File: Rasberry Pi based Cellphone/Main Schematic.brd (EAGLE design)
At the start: 100 x 80 mm, 124 parts, among them IC1 PCM2904DB, J1 Main B2B Header, J2 Second B2B Header, J3 Third B2B Header, Q1 20V P-Channel Mosfet, SW1 SPST_TACT-KMR2, SW2 SPST_TACT-KMR2, SW3 SPST_TACT-KMR2, X1 679105700, X2 679105700, X3 5036-008-210-862, X4 679105700

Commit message: random commit
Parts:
- added C45, C46, C47, C48: 10nF/25V, adafruit:C0402
- added C49: (no value), adafruit:R/2012-12R
- added C50: 10uF/6.3V, adafruit:R/2012-12R
- added R16: 10k, adafruit:M0805
- added R17: 2.2k, adafruit:M0805
- added U$6: MCP1702T-1502E/CB, Microchip_By_element14_Batch_1:SOT95P255X145-3N
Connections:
- removed net 3V2/NVCC_EIM2: Q1.2
- new net MSATA_DISABLE: R16.1, X1.20
- new net N$51: C45.1, X1.23
- new net N$59: C46.1, X1.25
- new net N$60: C47.1, X1.31
- new net N$61: C48.1, X1.33
- new net V_1V5: C50.+, R17.2, U$6.2, X1.28, X1.48, X1.6
- net 3V2/NVCC_EIM0: now also C49.+, Q1.2, R16.2, U$6.3, U1.23, X1.2, X1.24, X1.39, X1.41, X1.52
- net I2C1_SCL: now also X1.30
- net I2C1_SDA: now also X1.32
- net PE: now also C49.-, C50.-, R17.1, U$6.1, X1.15, X1.18, X1.21, X1.26, X1.27, X1.29, X1.34, X1.35, X1.37, X1.4, X1.40, X1.43, X1.50, X1.9
- net POR_B: now also X1.22
- net SATA_RXN: now also C46.2
- net SATA_RXP: now also C45.2
- net SATA_TXN: now also C47.2
- net SATA_TXP: now also C48.2

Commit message: almost finished schematic
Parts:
- removed X2, X4: 679105700, con-molex:679105700
- added C100, C101, C102, C104, C105, C106, C107, C108, C109, C110, C111, C112, C117, C118, C119, C120, C121, C122, C123, C124, C125, C126, C127, C59, C61, C62, C63, C69, C71, C72, C73, C74, C79, C81, C82, C83, C84, C89, C91, C92, C93, C98, C99: 0.1uF, resistor:C0402
- added C103, C113, C114, C115, C116, C60, C67, C70, C75, C78, C80, C85, C88, C90, C94, C95, C96, C97: 0.001uF, resistor:C0402
- added C51, C52: 10uF/6.3V, adafruit:R/2012-12R
- added C53, C54, C55, C56, C57, C58: 0.1uF/16V, adafruit:R/2012-12R
- added C66, C76, C86: 1.0uF, resistor:C0402
- added C68, C77, C87: 0.01uF, resistor:C0402
- added L10, L11, L4, L5, L6, L7: 1000@100MHz, dp_devices:FB402
- added L8: (no value), dp_devices:FB402
- added MSATA, PCIE1, PCIE2: 679105700, con-molex:679105700
- added R18, R19, R20, R22: 2.2k, adafruit:M0805
- added R21: 1kΩ, adafruit:M0805
- added RT13, RT14, RT17, RT18, RT21, RT22: 20Ω, adafruit:M0805
- added RT15, RT16, RT19, RT20, RT23, RT24: 49.9Ω, adafruit:M0805
- added RT25, RT26, RT27: 4.7kΩ, adafruit:M0805
- added RT28: 1.6kΩ, adafruit:M0805
- added U$7: MCP1700T-1502E/TT, Microchip_By_element14_Batch_1:SOT95P237X112-3N
- added U7: XIO3130_ZHC_196, texas:ZHC196
- X1: value 679105700 -> 5036-008-210-862; device con-molex:679105700 -> con-kyocera-elco:5036_008_210_862
- moved C49 602.6 mm to (45.7, 54.6)
- moved C50 602.6 mm to (45.7, 50.8)
- moved R17 602.6 mm to (45.7, 47.0)
- moved SW3 566.7 mm to (48.3, 55.9)
- moved U$6 566.7 mm to (52.1, 24.1)
- moved C45 566.7 mm to (47.0, 50.8)
- moved C46 566.7 mm to (47.0, 47.0)
- moved C47 566.7 mm to (47.0, 43.2)
- moved C48 566.7 mm to (47.0, 39.4)
- moved R16 566.7 mm to (48.3, 33.0)
- moved SW1 566.7 mm to (48.3, 63.5)
- moved SW2 566.7 mm to (48.3, 59.7)
- moved C44 520.3 mm to (27.9, 34.3)
- moved RN1 520.3 mm to (27.9, 26.7)
- moved C42 520.3 mm to (26.7, 52.1)
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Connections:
- removed net 3V2/NVCC_EIM0: ADC/DAC.20, ADC/DAC.5, C12.-, C17.+, C23.-, C49.+, J1.P$63, J1.P$65, J1.P$67, J1.P$69, L2.2, L3.1, Q1.2, R14.1, R16.2, RT5.2, SD2_VSELECT.7, SD2_VSELECT.8, U$2.3, U$6.3, U1.23, U1.34, U1.37, U1.38, U1.47, U4.P$5, U5.P$5, U6.P$5, X1.2, X1.24, X1.39, X1.41, X1.52
- new net 12C3_SDA: GPIOB.3
- new net 1V5: C102.1, C104.1, C105.1, C106.1, C107.1, C108.1, C109.1, C110.1, C111.1, C112.1, C113.1, C114.1, C115.1, C116.1, C117.1, C118.1, C119.1, C120.1, C121.1, C122.1, C123.1, C124.1, C125.1, C126.1, C127.1, C52.+, C59.1, C69.1, C79.1, C89.1, L4.1, L5.1, L6.1, L7.1, L8.1, PCIE1.28, PCIE1.48, PCIE1.6, PCIE2.28, PCIE2.48, PCIE2.6, R18.2, U$7.2, U7.A13, U7.A4, U7.B10, U7.B12, U7.B2, U7.B3, U7.B7, U7.C11, U7.C13, U7.C14, U7.C5, U7.E13, U7.F1, U7.F2, U7.G13, U7.H3, U7.K4, U7.L14, U7.M1, U7.M11, U7.M12, U7.M2, U7.N10, U7.N13, U7.N14, U7.N8, U7.P14, U7.P3, U7.P4
- new net 3V2: ADC/DAC.20, ADC/DAC.5, C100.1, C101.1, C12.-, C17.+, C23.-, C49.+, C51.+, C74.1, C84.1, C94.1, C95.1, C96.1, C97.1, C98.1, C99.1, GPIOA.1, GPIOB.1, J1.P$63, J1.P$65, J1.P$67, J1.P$69, L10.1, L11.1, L2.2, L3.1, MSATA.2, MSATA.24, MSATA.39, MSATA.41, MSATA.52, PCIE1.2, PCIE1.24, PCIE1.39, PCIE1.41, PCIE1.52, PCIE2.2, PCIE2.24, PCIE2.39, PCIE2.41, PCIE2.52, Q1.2, R14.1, R16.2, R19.1, R20.1, R21.2, R22.1, RT5.2, SD2_VSELECT.7, SD2_VSELECT.8, U$2.3, U$6.3, U$7.3, U1.23, U1.34, U1.37, U1.38, U1.47, U4.P$5, U5.P$5, U6.P$5, U7.A11, U7.A3, U7.B4, U7.D12, U7.D4, U7.K12, U7.M4, U7.N1, U7.P11
- new net DN1_PERST: PCIE1.22, RT27.2, U7.B5
- new net DN2_PERST: PCIE2.22, RT25.2, U7.A2
- new net DN3_PERST: RT26.2, U7.A1
- new net N$62: C54.-, PCIE2.31
- new net N$63: C53.-, PCIE2.33
- new net N$66: C56.-, PCIE1.31
- new net N$67: C55.-, PCIE1.33
- new net N$75: C57.+, U7.L2
- new net N$77: C58.+, U7.L1
- new net N$79: GPIOB.12
- new net N$80: GPIOB.13
- new net PCIE_RXM1: PCIE1.23, U7.B6
- new net PCIE_RXM2: PCIE2.23, U7.F14
- new net PCIE_RXM3: U7.P9
- new net PCIE_RXP1: PCIE1.25, U7.A6
- new net PCIE_RXP2: PCIE2.25, U7.F13
- new net PCIE_RXP3: U7.N9
- new net PCIE_TXM1: C56.+, U7.B8
- new net PCIE_TXM2: C54.+, U7.H14
- new net PCIE_TXM3: U7.P7
- new net PCIE_TXP1: C55.+
- new net PCIE_TXP2: C53.+, U7.H13
- new net PCIE_TXP3: U7.N7
- new net REFCLKN_1: PCIE1.11, RT14.2, RT16.1
- new net REFCLKN_1_R: RT14.1, U7.B9
- new net REFCLKN_2: PCIE2.11, RT22.2, RT24.1
- new net REFCLKN_2_R: RT22.1, U7.J14
- new net REFCLKN_3: RT18.2, RT20.1
- new net REFCLKN_3_R: RT18.1, U7.P6
- new net REFCLKP_1: PCIE1.13, RT13.2, RT15.1
- new net REFCLKP_1_R: RT13.1, U7.A9
- new net REFCLKP_2: PCIE2.13, RT21.2, RT23.1
- new net REFCLKP_2_R: RT21.1, U7.K14
- new net REFCLKP_3: RT17.2, RT19.1
- new net REFCLKP_3_R: RT17.1, U7.P5
- new net RXD0: GPIOA.9, R20.2, U4.P$3
- new net RXD1: GPIOA.11, R19.2, U5.P$3
- new net RXD2: GPIOA.13, R22.2, U6.P$3
- new net TXD0: GPIOA.8, U4.P$6
- new net TXD1: GPIOA.10, U5.P$6
- new net TXD2: GPIOA.12, U6.P$6
- new net UIM_AUX1_1: X3.C6
- new net UIM_AUX1_2: X1.C6
- new net UIM_AUX2_1: X3.C8
- new net UIM_AUX2_2: X1.C8
- new net UIM_CLK_1: PCIE1.12, X3.C2
- new net UIM_CLK_2: PCIE2.12, X1.C2
- new net UIM_DATA_1: PCIE1.10, X3.C4
- new net UIM_DATA_2: PCIE2.10, X1.C4
- new net UIM_PWR_1: PCIE1.8, X3.C1
- new net UIM_PWR_2: PCIE2.8, X1.C1
- new net UIM_RST_1: PCIE1.14, X3.C5
- new net UIM_RST_2: PCIE2.14, X1.C5
- new net UIM_VPP_1: PCIE1.16, X3.C7
- new net UIM_VPP_2: PCIE2.16, X1.C7
- new net VAUX33REF: R21.1, U7.E1
- new net VDD15REF: C103.1, L8.2, U7.F3
- new net VDD33REF: C85.1, L11.2, U7.E2
- new net VDDA15_0: C60.1, C61.1, C62.1, C63.1, L4.2, U7.G4, U7.H2, U7.H4, U7.J4, U7.K3
- new net VDDA15_1: C70.1, C71.1, C72.1, C73.1, L5.2, U7.A7, U7.D7, U7.D8, U7.D9
- new net VDDA15_2: C80.1, C81.1, C82.1, C83.1, L6.2, U7.G11, U7.G12, U7.H11, U7.J11, U7.J12
- new net VDDA15_3: C90.1, C91.1, C92.1, C93.1, L7.2, U7.L6, U7.L7, U7.L8, U7.M6, U7.M8
- new net VDDA33F: C75.1, L10.2, U7.J3
- new net VDDCOMB15: C86.1, C87.1, C88.1, U7.C1
- new net VDDCOMB33: C76.1, C77.1, C78.1, U7.F4
- new net VDDCOMBIO: C66.1, C67.1, C68.1, U7.D3
- net +5V: now also GPIOA.2, GPIOB.2
- net CLK1_N: now also C57.-
- net CLK1_P: now also C58.-
- net DISP1_DATA00: now also EXT_RADIO_INTERFACE.3
- net DISP1_DATA01: now also EXT_RADIO_INTERFACE.2
- net DISP1_DATA02: now also GPIOB.8
- net DISP1_DATA03: now also GPIOB.9
- net DISP1_DATA04: now also GPIOB.10
- net DISP1_DATA05: now also RT28.2, U7.B1
- net DISP1_DATA06: now also GPIOB.11
- net ECSPI2_MISO: now also GPIOA.4
- net ECSPI2_MOSI: now also GPIOA.3
- net ECSPI2_SCLK: now also GPIOA.5
- net ECSPI2_SS0: now also GPIOA.6
- net ECSPI2_SS1: now also GPIOA.7
- net I2C1_SCL: now also MSATA.30, U7.B14; no longer X1.30
- net I2C1_SDA: now also MSATA.32, U7.D13; no longer X1.32
- net I2C3_SCL: now also GPIOB.4
- net MSATA_DISABLE: now also MSATA.20, PCIE1.20, PCIE2.20; no longer X1.20
- net N$51: now also MSATA.23; no longer X1.23
- net N$59: now also MSATA.25; no longer X1.25
- net N$60: now also MSATA.31; no longer X1.31
- net N$61: now also MSATA.33; no longer X1.33
- net PCIE_RXM: now also U7.J2
- net PCIE_RXP: now also U7.J1
- net PCIE_TXM: now also U7.G2
- net PCIE_TXP: now also U7.A8, U7.G1
- net PE: now also C100.2, C101.2, C102.2, C103.2, C104.2, C105.2, C106.2, C107.2, C108.2, C109.2, C110.2, C111.2, C112.2, C113.2, C114.2, C115.2, C116.2, C117.2, C118.2, C119.2, C120.2, C121.2, C122.2, C123.2, C124.2, C125.2, C126.2, C127.2, C51.-, C52.-, C59.2, C60.2, C61.2, C62.2, C63.2, C66.2, C67.2, C68.2, C69.2, C70.2, C71.2, C72.2, C73.2, C74.2, C75.2, C76.2, C77.2, C78.2, C79.2, C80.2, C81.2, C82.2, C83.2, C84.2, C85.2, C86.2, C87.2, C88.2, C89.2, C90.2, C91.2, C92.2, C93.2, C94.2, C95.2, C96.2, C97.2, C98.2, C99.2, EXT_RADIO_INTERFACE.1, GPIOA.14, GPIOB.14, MSATA.15, MSATA.18, MSATA.21, MSATA.26, MSATA.27, MSATA.29, MSATA.34, MSATA.35, MSATA.37, MSATA.4, MSATA.40, MSATA.43, MSATA.50, MSATA.9, PCIE1.15, PCIE1.18, PCIE1.21, PCIE1.26, PCIE1.27, PCIE1.29, PCIE1.34, PCIE1.35, PCIE1.37, PCIE1.4, PCIE1.40, PCIE1.43, PCIE1.50, PCIE1.9, PCIE2.15, PCIE2.18, PCIE2.21, PCIE2.26, PCIE2.27, PCIE2.29, PCIE2.34, PCIE2.35, PCIE2.37, PCIE2.4, PCIE2.40, PCIE2.43, PCIE2.50, PCIE2.9, R18.1, RT15.2, RT16.2, RT19.2, RT20.2, RT23.2, RT24.2, RT25.1, RT26.1, RT27.1, RT28.1, U$7.1, U7.A10, U7.A5, U7.C10, U7.C4, U7.C7, U7.C8, U7.C9, U7.D1, U7.D10, U7.D11, U7.D5, U7.D6, U7.E10, U7.E11, U7.E12, U7.E14, U7.E4, U7.E5, U7.E6, U7.E7, U7.E8, U7.E9, U7.F10, U7.F11, U7.F12, U7.F5, U7.F6, U7.F7, U7.F8, U7.F9, U7.G10, U7.G14, U7.G3, U7.G5, U7.G6, U7.G7, U7.G8, U7.G9, U7.H1, U7.H10, U7.H12, U7.H5, U7.H6, U7.H7, U7.H8, U7.H9, U7.J10, U7.J13, U7.J5, U7.J6, U7.J7, U7.J8, U7.J9, U7.K1, U7.K10, U7.K11, U7.K13, U7.K2, U7.K5, U7.K6, U7.K7, U7.K8, U7.K9, U7.L10, U7.L11, U7.L13, U7.L4, U7.L5, U7.L9, U7.M5, U7.M7, U7.M9, U7.N4, U7.N5, U7.N6, U7.P1, U7.P10, U7.P8, X1.C3, X3.C3; no longer X1.15, X1.18, X1.21, X1.26, X1.27, X1.29, X1.34, X1.35, X1.37, X1.4, X1.40, X1.43, X1.50, X1.9
- net POR_B: now also MSATA.22; no longer X1.22
- net SD3_CLK: now also GPIOB.6
- net SD3_CMD: now also GPIOB.7
- net UART1_RX_DATA: now also U4.P$4
- net UART1_TX_DATA: now also U4.P$1
- net UART2_RX_DATA: now also U5.P$4
- net UART2_TX_DATA: now also U5.P$1
- net UART3_RX_DATA: now also U6.P$4
- net UART3_TX_DATA: now also U6.P$1
- net USB_OTG_ID: now also GPIOB.5
- net V_1V5: now also MSATA.28, MSATA.48, MSATA.6; no longer X1.28, X1.48, X1.6

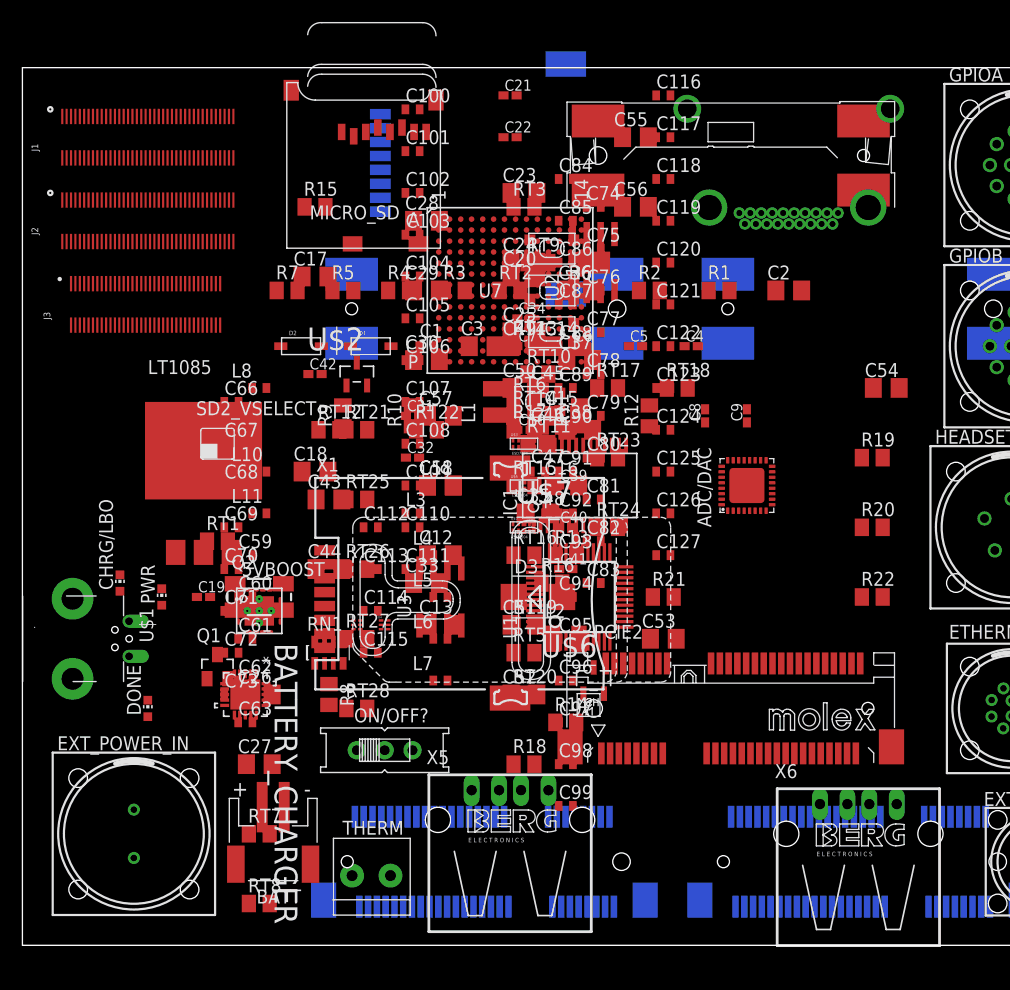
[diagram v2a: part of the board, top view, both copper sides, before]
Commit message: fixed some errors in schematic and made brd easier to look at
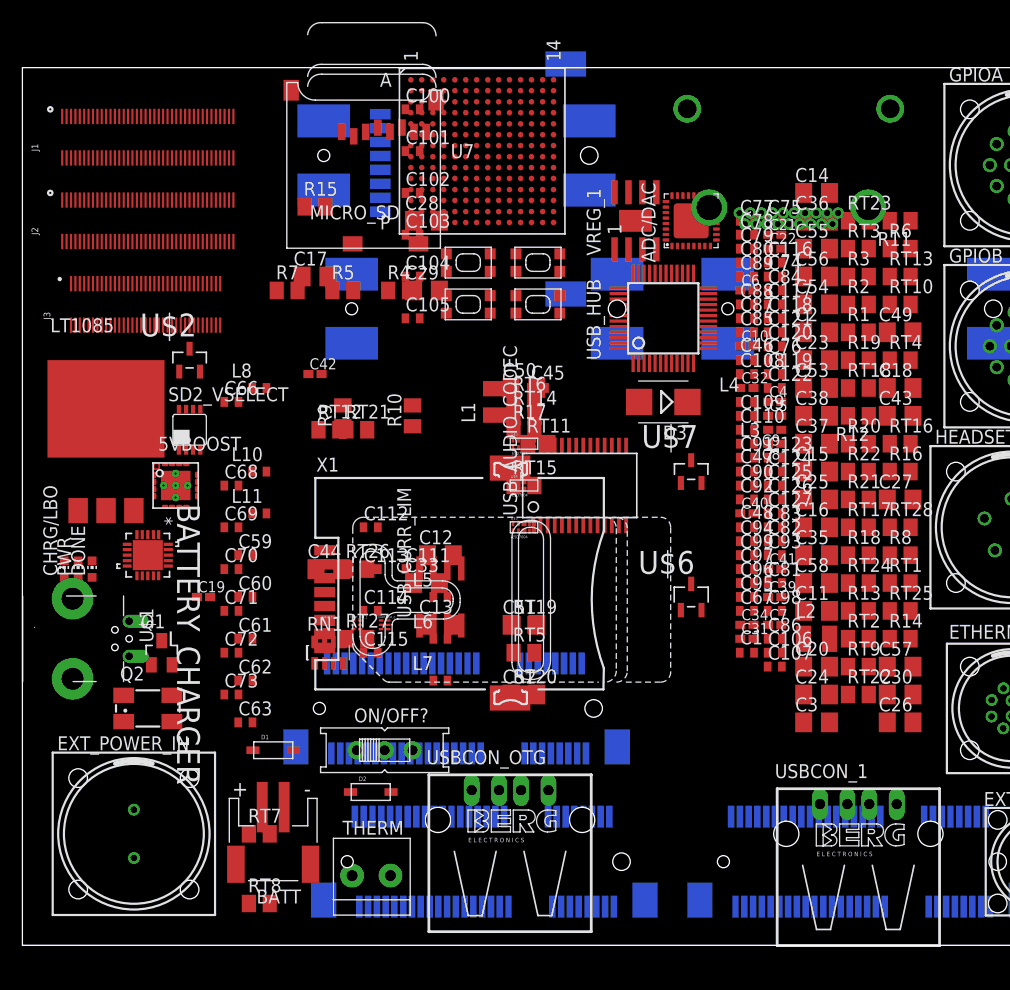
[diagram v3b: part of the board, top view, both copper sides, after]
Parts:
- removed U1: (no value), cypress:TQFP48_7X7
- removed U2: (no value), richtek:SOP08
- added USB_HUB: USB Hub, cypress:TQFP48_7X7
- added VREG_1: +5V -> 3V2, richtek:SOP08
- C1: value (none) -> 1uF
- C3, C49: value (none) -> 10uF/6.3V
- D3: value (none) -> RB521CS-30
- L8: value (none) -> 1000@100MHz
- Q2: value (none) -> 12MHz
- UART_BUF_0, UART_BUF_1, UART_BUF_2: value (none) -> NLX2G16
- USBCON_1: value (none) -> USB_1
- USBCON_OTG: value (none) -> USB_OTG
- USB_CURR_LIM: value (none) -> MIC2026-1YM
- moved C27 63.2 mm to (80.0, 40.6)
- moved RT1 62.3 mm to (80.0, 33.0)
- moved C26 58.5 mm to (80.0, 20.3)
- moved C18 53.9 mm to (80.0, 50.8)
- moved R8 53.6 mm to (80.0, 35.6), turned to 0 degrees
- moved C30 52.9 mm to (80.0, 22.9)
- moved C43 52.6 mm to (80.0, 48.3)
- moved RT28 52.2 mm to (80.0, 38.1)
- moved RT25 50.6 mm to (80.0, 30.5)
- moved C67 49.4 mm to (66.0, 30.5)
- moved C57 47.7 mm to (80.0, 25.4)
- moved C24 47.6 mm to (72.4, 22.9)
- moved RT9 47.0 mm to (76.2, 25.4)
- moved RT22 46.2 mm to (76.2, 22.9)
- moved C3 45.9 mm to (72.4, 20.3)
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- renumbered IC1 to USB_AUDIO_CODEC, U3 to USB_CURR_LIM, U4 to UART_BUF_0, U5 to UART_BUF_1, U6 to UART_BUF_2, X5 to USBCON_OTG, X6 to USBCON_1
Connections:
- net VCC_1V8 renamed 1V8
- new net LVDS0_TX2_P: J2.P$74
- new net VCC: USB_HUB.47
- net +5V: now also VREG_1.4; no longer U2.4
- net 3V2: now also USB_HUB.23, USB_HUB.34, USB_HUB.37, USB_HUB.38; no longer U1.23, U1.34, U1.37, U1.38, U1.47
- net AUD5_TXD: now also J2.P$53
- net N$19: now also VREG_1.7; no longer U2.7
- net N$25: now also VREG_1.2; no longer U2.2
- net N$27: now also VREG_1.1; no longer U2.1
- net N$34: now also USB_HUB.11; no longer U1.11
- net N$35: now also USB_HUB.39; no longer U1.39
- net N$7: now also VREG_1.5; no longer U2.5
- net PE: now also J2.P$12, USB_HUB.13, USB_HUB.2, USB_HUB.20, USB_HUB.8, VREG_1.P$1; no longer U1.13, U1.2, U1.20, U1.8, U2.P$1
- net POR_B: now also USB_HUB.26; no longer U1.26
- net USB_HOST_DN: now also USB_HUB.3; no longer U1.3
- net USB_HOST_DP: now also USB_HUB.4; no longer U1.4
- net USB_HUB_DN1: now also USB_HUB.5; no longer U1.5
- net USB_HUB_DN2: now also PCIE1.36, USB_HUB.9; no longer U1.9
- net USB_HUB_DN3: now also PCIE2.36, USB_HUB.17; no longer U1.17
- net USB_HUB_DN4: now also USB_HUB.21; no longer U1.21
- net USB_HUB_DP1: now also USB_HUB.6; no longer U1.6
- net USB_HUB_DP2: now also PCIE1.38, USB_HUB.10; no longer U1.10
- net USB_HUB_DP3: now also PCIE2.38, USB_HUB.18; no longer U1.18
- net USB_HUB_DP4: now also USB_HUB.22; no longer U1.22
- net V_3V2_FLTR: now also USB_HUB.1, USB_HUB.12, USB_HUB.16, USB_HUB.19, USB_HUB.48, USB_HUB.7; no longer U1.1, U1.12, U1.16, U1.19, U1.48, U1.7
- net XIN: now also USB_HUB.14; no longer U1.14
- net XOUT: now also USB_HUB.15; no longer U1.15
